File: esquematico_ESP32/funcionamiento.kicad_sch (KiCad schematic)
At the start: 9 parts, among them J7 Jack-DC, U2 LM1117-3.3

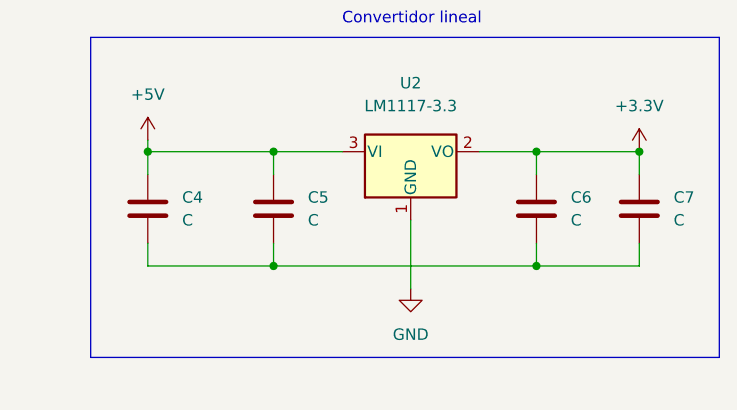
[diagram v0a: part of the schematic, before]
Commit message: ruteo listo con un posible error en footprint esp32
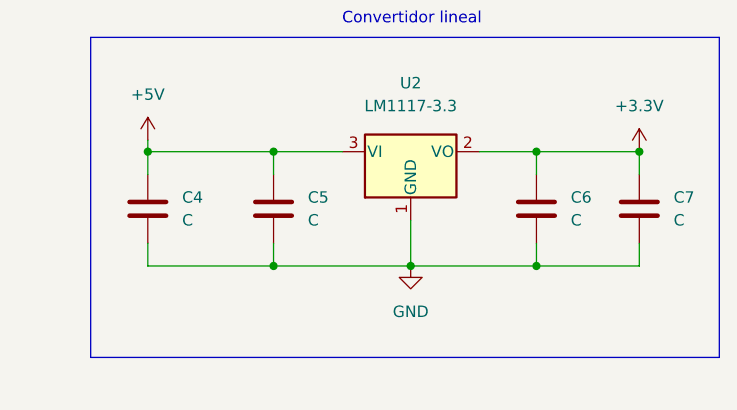
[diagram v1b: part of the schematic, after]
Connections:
- net GND: now also C4.2, C5.2, C6.2, C7.2
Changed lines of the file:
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@@
   (junction (at 224.79 82.55) (diameter 0) (color 0 0 0 0)
   )
+  (junction (at 210.82 82.55) (diameter 0) (color 0 0 0 0)
+  )
   (junction (at 236.22 69.85) (diameter 0) (color 0 0 0 0)
   )
@@
     (stroke (width 0) (type default) (color 0 0 0 0))
   )
-  (wire (pts (xy 195.58 82.55) (xy 224.79 82.55))
+  (wire (pts (xy 195.58 82.55) (xy 210.82 82.55))
+    (stroke (width 0) (type default) (color 0 0 0 0))
+  )
+  (wire (pts (xy 210.82 82.55) (xy 224.79 82.55))
     (stroke (width 0) (type default) (color 0 0 0 0))
   )
@@
     (stroke (width 0) (type default) (color 0 0 0 0))
   )
-  (wire (pts (xy 210.82 77.47) (xy 210.82 85.09))
+  (wire (pts (xy 210.82 77.47) (xy 210.82 82.55))
     (stroke (width 0) (type default) (color 0 0 0 0))
   )
@@
     (pin "2")
   )
-  (symbol (lib_id "power:GND") (at 210.82 85.09 0) (unit 1)
-    (in_bom yes) (on_board yes) (fields_autoplaced)
-    (property "Reference" "#PWR040" (id 0) (at 210.82 91.44 0)
-      (effects (font (size 1.27 1.27)) hide)
-    )
-    (property "Value" "GND" (id 1) (at 210.82 90.17 0))
-    (property "Footprint" "" (id 2) (at 210.82 85.09 0)
-      (effects (font (size 1.27 1.27)) hide)
-    )
-    (property "Datasheet" "" (id 3) (at 210.82 85.09 0)
-      (effects (font (size 1.27 1.27)) hide)
-    )
+  (symbol (lib_id "power:GND") (at 210.82 82.55 0) (unit 1)
+    (in_bom yes) (on_board yes) (fields_autoplaced)
+    (property "Reference" "#PWR040" (id 0) (at 210.82 88.9 0)
+      (effects (font (size 1.27 1.27)) hide)
+    )
+    (property "Value" "GND" (id 1) (at 210.82 87.63 0))
+    (property "Footprint" "" (id 2) (at 210.82 82.55 0)
+      (effects (font (size 1.27 1.27)) hide)
+    )
+    (property "Datasheet" "" (id 3) (at 210.82 82.55 0)
+      (effects (font (size 1.27 1.27)) hide)
+    )

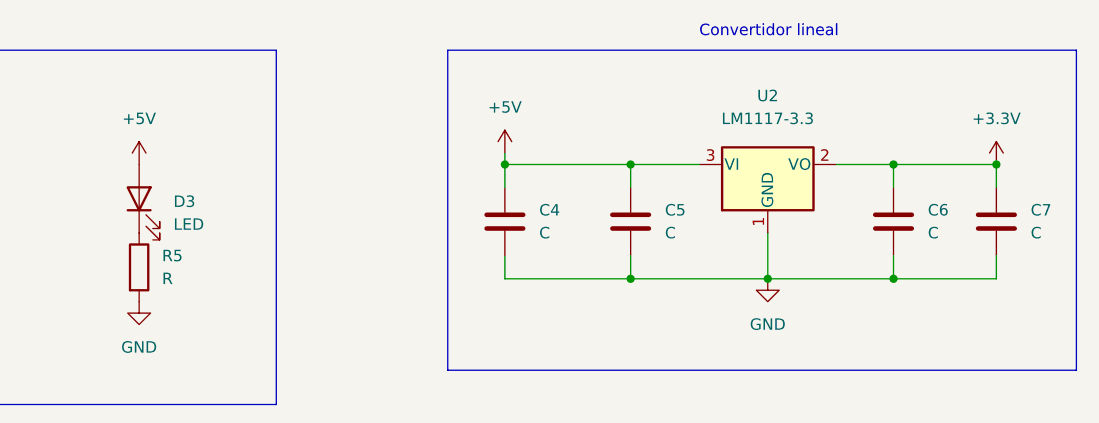
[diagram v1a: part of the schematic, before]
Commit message: se agregaron los valores (pendiente última revisión)
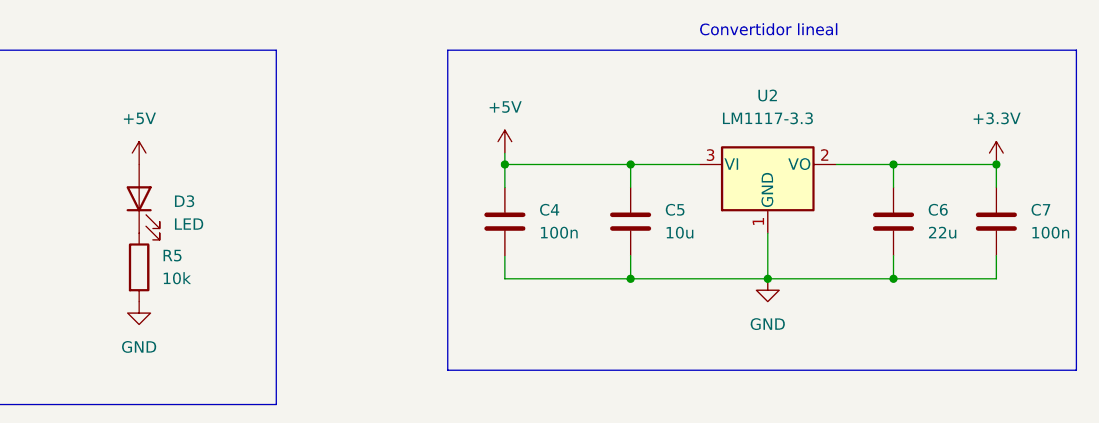
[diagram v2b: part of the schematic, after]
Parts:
- C4, C7: value C -> 100n
- C5: value C -> 10u
- C6: value C -> 22u
- R5: value R -> 10k
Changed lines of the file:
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@@
       (effects (font (size 1.27 1.27)) (justify left))
     )
-    (property "Value" "C" (id 1) (at 240.03 77.4699 0)
+    (property "Value" "100n" (id 1) (at 240.03 77.4699 0)
       (effects (font (size 1.27 1.27)) (justify left))
     )
@@
       (effects (font (size 1.27 1.27)) (justify left))
     )
-    (property "Value" "C" (id 1) (at 185.42 77.4699 0)
+    (property "Value" "100n" (id 1) (at 185.42 77.4699 0)
       (effects (font (size 1.27 1.27)) (justify left))
     )
@@
       (effects (font (size 1.27 1.27)) (justify left))
     )
-    (property "Value" "C" (id 1) (at 199.39 77.4699 0)
+    (property "Value" "10u" (id 1) (at 199.39 77.4699 0)
       (effects (font (size 1.27 1.27)) (justify left))
     )
@@
       (effects (font (size 1.27 1.27)) (justify left))
     )
-    (property "Value" "R" (id 1) (at 143.51 82.5499 0)
+    (property "Value" "10k" (id 1) (at 143.51 82.5499 0)
       (effects (font (size 1.27 1.27)) (justify left))
     )
@@
       (effects (font (size 1.27 1.27)) (justify left))
     )
-    (property "Value" "C" (id 1) (at 228.6 77.4699 0)
+    (property "Value" "22u" (id 1) (at 228.6 77.4699 0)
       (effects (font (size 1.27 1.27)) (justify left))
     )

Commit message: Correciones de la clase
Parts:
- added verificación1: Conn_01x03_Male, Connector_PinHeader_2.54mm:PinHeader_1x03_P2.54mm_Vertical, symbol Connector:Conn_01x03_Male
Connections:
- net +3V3: now also verificación1.2 (Pin_2)
- net +5V: now also verificación1.1 (Pin_1)
- net GND: now also verificación1.3 (Pin_3)
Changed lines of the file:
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@@
+    (stroke (width 0) (type default) (color 0 0 0 0))
+  )
+  (polyline (pts (xy 79.375 107.95) (xy 133.985 107.95))
     (stroke (width 0) (type default) (color 0 0 0 0))
   )
@@
     (stroke (width 0) (type default) (color 0 0 0 0))
   )
+  (polyline (pts (xy 133.985 107.95) (xy 133.985 128.905))
+    (stroke (width 0) (type default) (color 0 0 0 0))
+  )
   (wire (pts (xy 236.22 82.55) (xy 224.79 82.55))
     (stroke (width 0) (type default) (color 0 0 0 0))
@@
     (stroke (width 0) (type default) (color 0 0 0 0))
   )
+  (polyline (pts (xy 133.985 128.905) (xy 78.74 128.905))
+    (stroke (width 0) (type default) (color 0 0 0 0))
+  )
   (polyline (pts (xy 175.26 92.71) (xy 245.11 92.71))
     (stroke (width 0) (type default) (color 0 0 0 0))
   )
   (wire (pts (xy 82.55 81.28) (xy 82.55 82.55))
+    (stroke (width 0) (type default) (color 0 0 0 0))
+  )
+  (polyline (pts (xy 78.74 128.905) (xy 78.74 107.95))
     (stroke (width 0) (type default) (color 0 0 0 0))
   )
@@
   (text "Regulador\n" (at 101.6 55.88 0)
     (effects (font (size 1.27 1.27)) (justify left bottom))
+  )
+  (symbol (lib_id "power:+3.3V") (at 104.775 120.65 270) (unit 1)
+    (in_bom yes) (on_board yes) (fields_autoplaced)
+    (property "Reference" "#PWR0106" (id 0) (at 100.965 120.65 0)
+      (effects (font (size 1.27 1.27)) hide)
+    )
+    (property "Value" "+3.3V" (id 1) (at 107.95 120.6499 90)
+      (effects (font (size 1.27 1.27)) (justify left))
+    )
+    (property "Footprint" "" (id 2) (at 104.775 120.65 0)
+      (effects (font (size 1.27 1.27)) hide)
+    )
+    (property "Datasheet" "" (id 3) (at 104.775 120.65 0)
+      (effects (font (size 1.27 1.27)) hide)
+    )
+    (pin "1")
   )
   (symbol (lib_id "Device:C") (at 236.22 76.2 0) (unit 1)
@@
     )
     (property "Datasheet" "" (id 3) (at 82.55 82.55 0)
+      (effects (font (size 1.27 1.27)) hide)
+    )
+    (pin "1")
+  )
+  (symbol (lib_id "power:GND") (at 104.775 123.19 90) (unit 1)
+    (in_bom yes) (on_board yes) (fields_autoplaced)
+    (property "Reference" "#PWR0107" (id 0) (at 111.125 123.19 0)
+      (effects (font (size 1.27 1.27)) hide)
+    )
+    (property "Value" "GND" (id 1) (at 107.95 123.1899 90)
+      (effects (font (size 1.27 1.27)) (justify right))
+    )
+    (property "Footprint" "" (id 2) (at 104.775 123.19 0)
+      (effects (font (size 1.27 1.27)) hide)
+    )
+    (property "Datasheet" "" (id 3) (at 104.775 123.19 0)
       (effects (font (size 1.27 1.27)) hide)
     )
@@
     (pin "1")
   )
+  (symbol (lib_id "power:+5V") (at 104.775 118.11 270) (unit 1)
+    (in_bom yes) (on_board yes) (fields_autoplaced)
+    (property "Reference" "#PWR0105" (id 0) (at 100.965 118.11 0)
+      (effects (font (size 1.27 1.27)) hide)
+    )
+    (property "Value" "+5V" (id 1) (at 107.95 118.1099 90)
+      (effects (font (size 1.27 1.27)) (justify left))
+    )
+    (property "Footprint" "" (id 2) (at 104.775 118.11 0)
+      (effects (font (size 1.27 1.27)) hide)
+    )
+    (property "Datasheet" "" (id 3) (at 104.775 118.11 0)
+      (effects (font (size 1.27 1.27)) hide)
+    )
+    (pin "1")
+  )
+  (symbol (lib_id "Connector:Conn_01x03_Male") (at 99.695 120.65 0) (unit 1)
+    (in_bom yes) (on_board yes) (fields_autoplaced)
+    (property "Reference" "verificación1" (id 0) (at 100.33 113.03 0))
+    (property "Value" "Conn_01x03_Male" (id 1) (at 100.33 115.57 0))
+    (property "Footprint" "Connector_PinHeader_2.54mm:PinHeader_1x03_P2.54mm_Vertical" (id 2) (at 99.695 120.65 0)
+      (effects (font (size 1.27 1.27)) hide)
+    )
+    (property "Datasheet" "~" (id 3) (at 99.695 120.65 0)
+      (effects (font (size 1.27 1.27)) hide)
+    )
+    (pin "1")
+    (pin "2")
+    (pin "3")
+  )
   (symbol (lib_id "Connector:Jack-DC") (at 54.61 78.74 0) (unit 1)

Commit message: huecos listos
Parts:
- removed verificación1: Conn_01x03_Male, Connector_PinHeader_2.54mm:PinHeader_1x03_P2.54mm_Vertical, symbol Connector:Conn_01x03_Male
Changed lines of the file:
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@@
-    (stroke (width 0) (type default) (color 0 0 0 0))
-  )
-  (polyline (pts (xy 79.375 107.95) (xy 133.985 107.95))
     (stroke (width 0) (type default) (color 0 0 0 0))
   )
@@
     (stroke (width 0) (type default) (color 0 0 0 0))
   )
-  (polyline (pts (xy 133.985 107.95) (xy 133.985 128.905))
-    (stroke (width 0) (type default) (color 0 0 0 0))
-  )
   (wire (pts (xy 236.22 82.55) (xy 224.79 82.55))
     (stroke (width 0) (type default) (color 0 0 0 0))
@@
     (stroke (width 0) (type default) (color 0 0 0 0))
   )
-  (polyline (pts (xy 133.985 128.905) (xy 78.74 128.905))
-    (stroke (width 0) (type default) (color 0 0 0 0))
-  )
   (polyline (pts (xy 175.26 92.71) (xy 245.11 92.71))
     (stroke (width 0) (type default) (color 0 0 0 0))
   )
   (wire (pts (xy 82.55 81.28) (xy 82.55 82.55))
-    (stroke (width 0) (type default) (color 0 0 0 0))
-  )
-  (polyline (pts (xy 78.74 128.905) (xy 78.74 107.95))
     (stroke (width 0) (type default) (color 0 0 0 0))
   )
@@
   (text "Regulador\n" (at 101.6 55.88 0)
     (effects (font (size 1.27 1.27)) (justify left bottom))
-  )
-  (symbol (lib_id "power:+3.3V") (at 104.775 120.65 270) (unit 1)
-    (in_bom yes) (on_board yes) (fields_autoplaced)
-    (property "Reference" "#PWR0106" (id 0) (at 100.965 120.65 0)
-      (effects (font (size 1.27 1.27)) hide)
-    )
-    (property "Value" "+3.3V" (id 1) (at 107.95 120.6499 90)
-      (effects (font (size 1.27 1.27)) (justify left))
-    )
-    (property "Footprint" "" (id 2) (at 104.775 120.65 0)
-      (effects (font (size 1.27 1.27)) hide)
-    )
-    (property "Datasheet" "" (id 3) (at 104.775 120.65 0)
-      (effects (font (size 1.27 1.27)) hide)
-    )
-    (pin "1")
   )
   (symbol (lib_id "Device:C") (at 236.22 76.2 0) (unit 1)
@@
     )
     (property "Datasheet" "" (id 3) (at 82.55 82.55 0)
-      (effects (font (size 1.27 1.27)) hide)
-    )
-    (pin "1")
-  )
-  (symbol (lib_id "power:GND") (at 104.775 123.19 90) (unit 1)
-    (in_bom yes) (on_board yes) (fields_autoplaced)
-    (property "Reference" "#PWR0107" (id 0) (at 111.125 123.19 0)
-      (effects (font (size 1.27 1.27)) hide)
-    )
-    (property "Value" "GND" (id 1) (at 107.95 123.1899 90)
-      (effects (font (size 1.27 1.27)) (justify right))
-    )
-    (property "Footprint" "" (id 2) (at 104.775 123.19 0)
-      (effects (font (size 1.27 1.27)) hide)
-    )
-    (property "Datasheet" "" (id 3) (at 104.775 123.19 0)
       (effects (font (size 1.27 1.27)) hide)
     )
@@
     (pin "1")
   )
-  (symbol (lib_id "power:+5V") (at 104.775 118.11 270) (unit 1)
-    (in_bom yes) (on_board yes) (fields_autoplaced)
-    (property "Reference" "#PWR0105" (id 0) (at 100.965 118.11 0)
-      (effects (font (size 1.27 1.27)) hide)
-    )
-    (property "Value" "+5V" (id 1) (at 107.95 118.1099 90)
-      (effects (font (size 1.27 1.27)) (justify left))
-    )
-    (property "Footprint" "" (id 2) (at 104.775 118.11 0)
-      (effects (font (size 1.27 1.27)) hide)
-    )
-    (property "Datasheet" "" (id 3) (at 104.775 118.11 0)
-      (effects (font (size 1.27 1.27)) hide)
-    )
-    (pin "1")
-  )
-  (symbol (lib_id "Connector:Conn_01x03_Male") (at 99.695 120.65 0) (unit 1)
-    (in_bom yes) (on_board yes) (fields_autoplaced)
-    (property "Reference" "verificación1" (id 0) (at 100.33 113.03 0))
-    (property "Value" "Conn_01x03_Male" (id 1) (at 100.33 115.57 0))
-    (property "Footprint" "Connector_PinHeader_2.54mm:PinHeader_1x03_P2.54mm_Vertical" (id 2) (at 99.695 120.65 0)
-      (effects (font (size 1.27 1.27)) hide)
-    )
-    (property "Datasheet" "~" (id 3) (at 99.695 120.65 0)
-      (effects (font (size 1.27 1.27)) hide)
-    )
-    (pin "1")
-    (pin "2")
-    (pin "3")
-  )
   (symbol (lib_id "Connector:Jack-DC") (at 54.61 78.74 0) (unit 1)

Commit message: Alternativa_Acomodada
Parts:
- D3: footprint LED_SMD:LED_1206_3216Metric_Pad1.42x1.75mm_HandSolder -> LED_SMD:LED_0805_2012Metric_Pad1.15x1.40mm_HandSolder
- renumbered J7 to Vin1
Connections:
- net at FB2.2, Vin1.2: now also Vin1.3
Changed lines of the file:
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@@
   (junction (at 195.58 69.85) (diameter 0) (color 0 0 0 0)
   )
+  (junction (at 64.77 81.28) (diameter 0) (color 0 0 0 0)
+  )
   (junction (at 224.79 82.55) (diameter 0) (color 0 0 0 0)
   )
@@
   (junction (at 224.79 69.85) (diameter 0) (color 0 0 0 0)
   )
-  (wire (pts (xy 62.23 81.28) (xy 71.12 81.28))
+  (wire (pts (xy 62.23 81.28) (xy 64.77 81.28))
     (stroke (width 0) (type default) (color 0 0 0 0))
   )
@@
     (stroke (width 0) (type default) (color 0 0 0 0))
   )
+  (wire (pts (xy 64.77 78.74) (xy 64.77 81.28))
+    (stroke (width 0) (type default) (color 0 0 0 0))
+  )
   (wire (pts (xy 181.61 69.85) (xy 181.61 72.39))
     (stroke (width 0) (type default) (color 0 0 0 0))
@@
     (stroke (width 0) (type default) (color 0 0 0 0))
   )
+  (wire (pts (xy 62.23 78.74) (xy 64.77 78.74))
+    (stroke (width 0) (type default) (color 0 0 0 0))
+  )
   (wire (pts (xy 78.74 81.28) (xy 82.55 81.28))
+    (stroke (width 0) (type default) (color 0 0 0 0))
+  )
+  (wire (pts (xy 64.77 81.28) (xy 71.12 81.28))
     (stroke (width 0) (type default) (color 0 0 0 0))
   )
@@
   (symbol (lib_id "Connector:Jack-DC") (at 54.61 78.74 0) (unit 1)
     (in_bom yes) (on_board yes) (fields_autoplaced)
-    (property "Reference" "J7" (id 0) (at 54.61 69.85 0))
+    (property "Reference" "Vin1" (id 0) (at 54.61 69.85 0))
     (property "Value" "Jack-DC" (id 1) (at 54.61 72.39 0))
     (property "Footprint" "Connector_BarrelJack:BarrelJack_Horizontal" (id 2) (at 55.88 79.756 0)
@@
     (pin "1")
     (pin "2")
+    (pin "3")
   )
   (symbol (lib_id "Device:C") (at 195.58 76.2 0) (unit 1)
@@
       (effects (font (size 1.27 1.27)) (justify right))
     )
-    (property "Footprint" "LED_SMD:LED_1206_3216Metric_Pad1.42x1.75mm_HandSolder" (id 2) (at 140.97 73.66 0)
-      (effects (font (size 1.27 1.27)) hide)
-    )
+    (property "Footprint" "LED_SMD:LED_0805_2012Metric_Pad1.15x1.40mm_HandSolder" (id 2) (at 140.97 73.66 0)
+      (effects (font (size 1.27 1.27)) hide)
+    )
